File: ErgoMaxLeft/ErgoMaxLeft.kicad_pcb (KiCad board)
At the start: 2 copper layers, 182.8 x 169.2 mm, 103 parts, among them J1 PJ-320A, K1 F1, K10 3 #, K11 4 $, K12 5 %, K13 KEYSW, K14 KEYSW, K15 Q, K16 W, K17 E, K18 R, K19 T, K2 F2, K20 KEYSW, K21 KEYSW, K22 A, K23 S, K24 D, K25 F, K26 G, K27 KEYSW, K28 KEYSW, K29 KEYSW, K3 F3, K30 Z, K31 X, K32 C, K33 V, K34 B, K35 KEYSW, K36 KEYSW, K37 KEYSW, K38 KEYSW, K39 KEYSW, K4 F4, K40 KEYSW, K41 KEYSW, K42 KEYSW, K43 KEYSW, K44 KEYSW, K5 F5, K6 F1, K7 KEYSW, K8 1 !, K9 2 @, U1 ProMicro

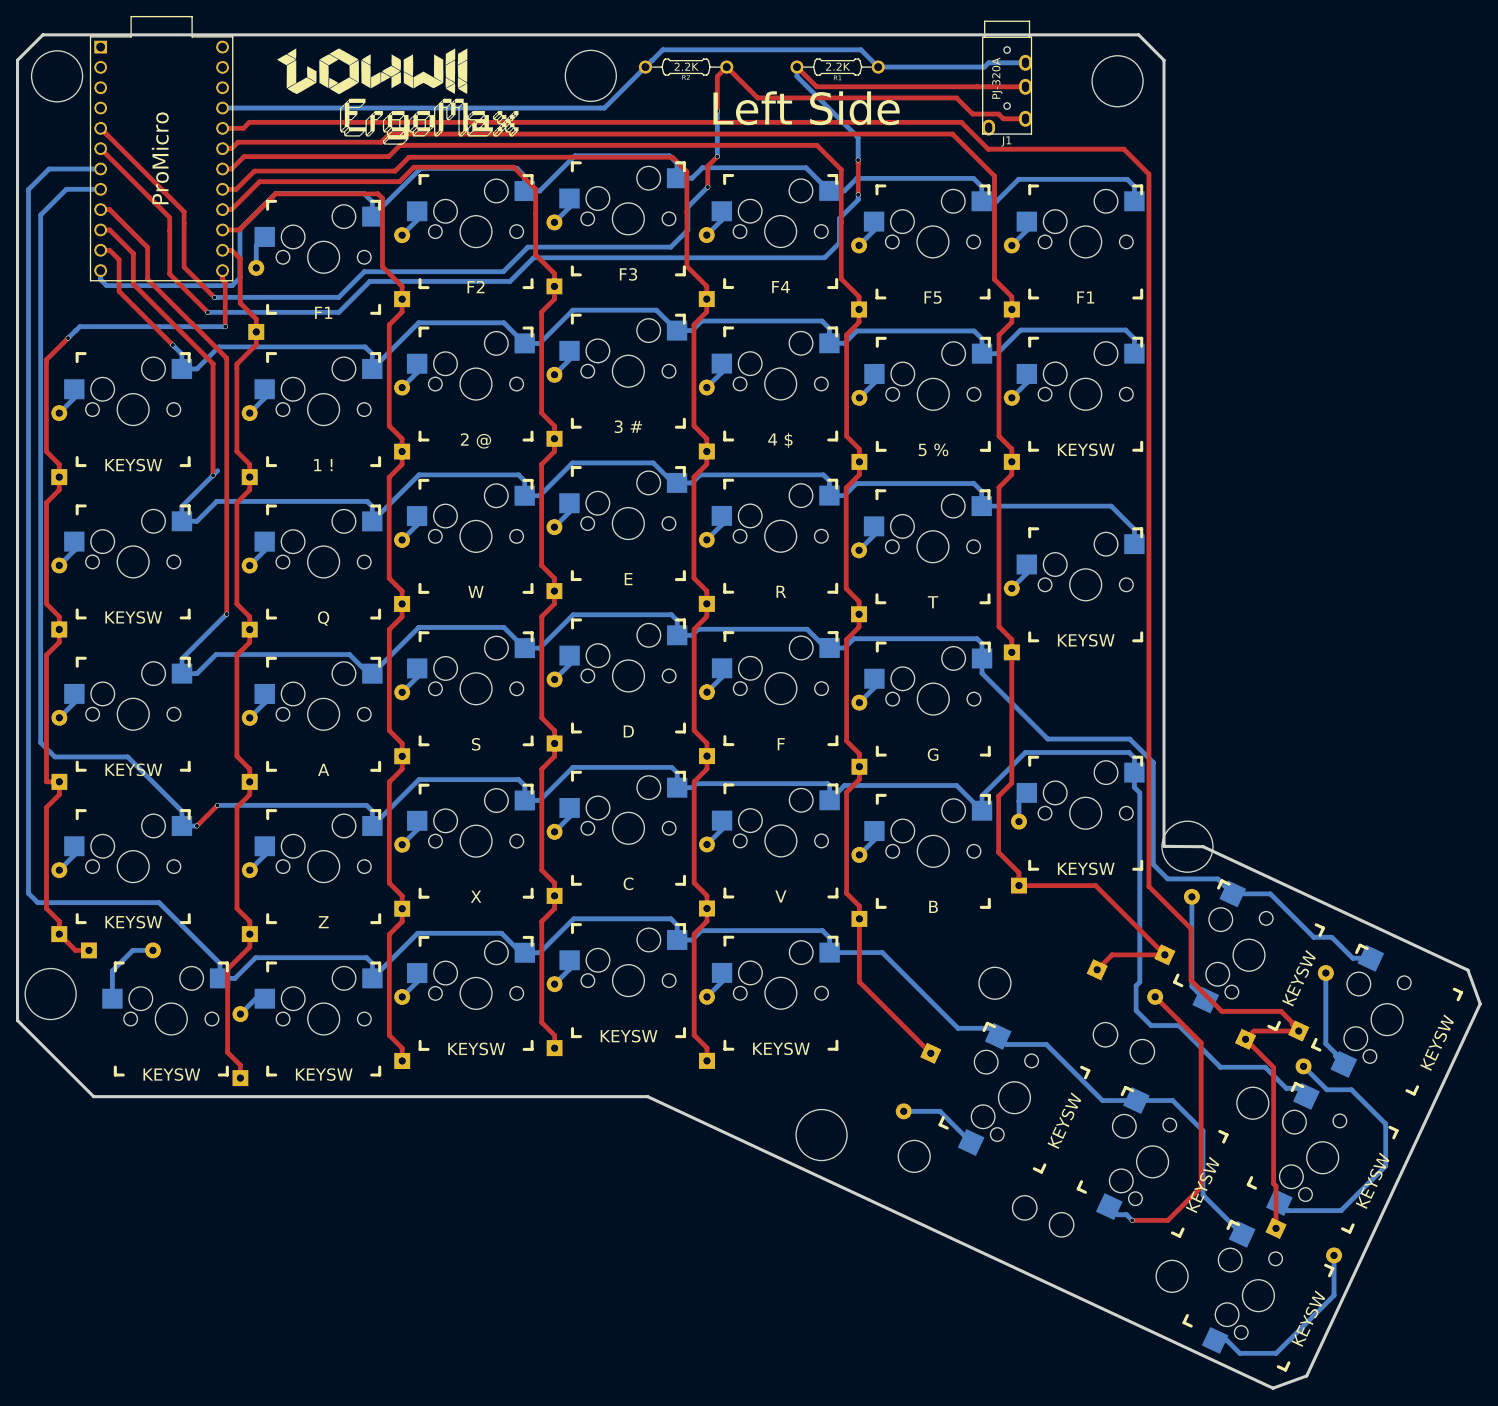
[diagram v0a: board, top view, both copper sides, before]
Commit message: feat: using smd components for the diodes and the resistor
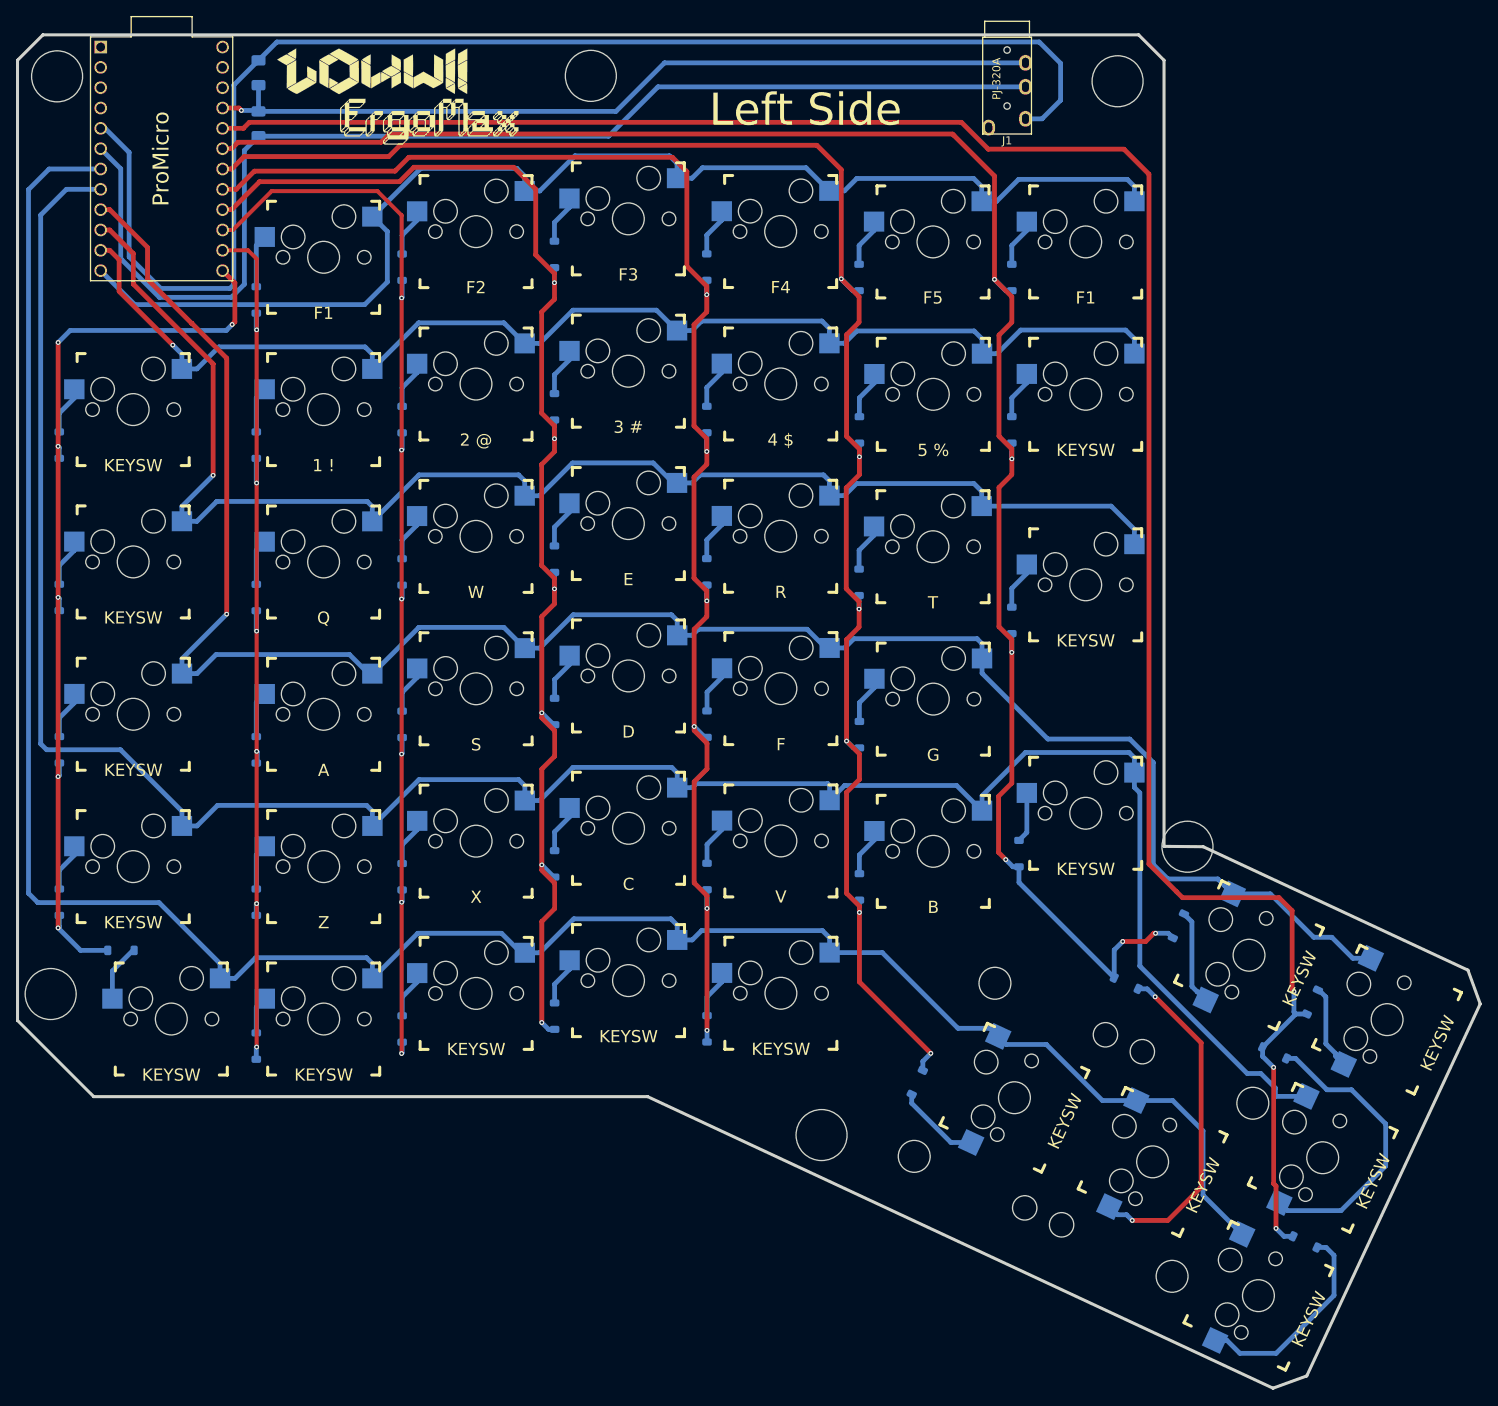
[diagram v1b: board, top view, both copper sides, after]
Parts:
- D1, D10, D11, D12, D13, D14, D15, D16, D17, D18, D19, D2, D20, D21, D22, D23, D24, D25, D26, D27, D28, D29, D3, D30, D31, D32, D33, D34, D35, D36, D37, D38, D39, D4, D40, D41, D42, D43, D44, D5, D6, D7, D8, D9: footprint Keebio-Parts:Diode_Long -> Diode_SMD:D_SOD-123
- R1, R2: footprint Keebio-Parts:Resistor -> Resistor_SMD:R_1206_3216Metric_Pad1.30x1.75mm_HandSolder
- moved R1 72.7 mm to (140.5, 47.0), turned to 90 degrees
- moved R2 53.5 mm to (140.5, 40.6), turned to -90 degrees
- moved D38 1.98 mm to (140.2, 162.3), turned to 90 degrees
- moved D15 0.82 mm to (140.2, 106.2), turned to 90 degrees
- moved D8 0.82 mm to (140.2, 87.1), turned to 90 degrees
- moved D22 0.82 mm to (140.2, 125.2), turned to 90 degrees
- moved D30 0.81 mm to (140.2, 144.3), turned to 90 degrees
- turned D23 to 90 degrees
- turned D31 to 90 degrees
- turned D39 to 90 degrees
- turned D2 to 90 degrees
- turned D16 to 90 degrees
- turned D1 to 90 degrees
- turned D10 to 90 degrees
- turned D11 to 90 degrees
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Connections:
- U1 pad 1: Net-(U1-Pad1) -> unconnected-(U1-TX-Pad1)
- U1 pad 2: Net-(U1-Pad2) -> unconnected-(U1-RX-Pad2)
- U1 pad 22: Net-(U1-Pad22) -> unconnected-(U1-RST-Pad22)
- U1 pad 24: Net-(U1-Pad24) -> unconnected-(U1-RAW-Pad24)
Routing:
- net SDA: track 152.1 -> 174.4 mm, vias 4 -> 0
- net SCL: track 164.3 -> 150.6 mm, vias 3 -> 0
- net /Col5: track 200.2 -> 212.5 mm, vias 0 -> 6
- net /Col3: track 157.5 -> 166.3 mm, vias 0 -> 6
- net /Col4: track 179.2 -> 186.2 mm, vias 0 -> 6
- net /Col6: track 224.5 -> 229.3 mm, vias 0 -> 6
- net /Col0: track 113.1 -> 117.4 mm, vias 2 -> 6
- net /Col2: track 137.6 -> 141.7 mm, vias 0 -> 6
- net /Row4: track 294.9 -> 291.7 mm, vias 2 -> 0
- net Net-(D36-A): track 34.5 -> 37.1 mm
- net Net-(D43-A): track 40.1 -> 42.6 mm, vias 1 -> 2
- net Net-(D44-A): track 23.5 -> 26.1 mm
- net Net-(D37-A): track 9.60 -> 7.10 mm
- net Net-(D16-A): track 3.76 -> 6.11 mm
- net Net-(D41-A): track 3.76 -> 6.11 mm
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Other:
- copper layers 2 -> 4
- net class Default removed
- rule pad_to_mask_clearance: 0.051 -> 0
